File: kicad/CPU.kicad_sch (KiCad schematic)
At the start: 37 parts, among them J1 Conn_ARM_SWD_TagConnect_TC203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, J2 Screw_Terminal_01x03, J3 Screw_Terminal_01x03, SW1 SW_Push, U7 STM32F303CBTx, U8 ATA6560-GAQW-N, Y1 8 MHz

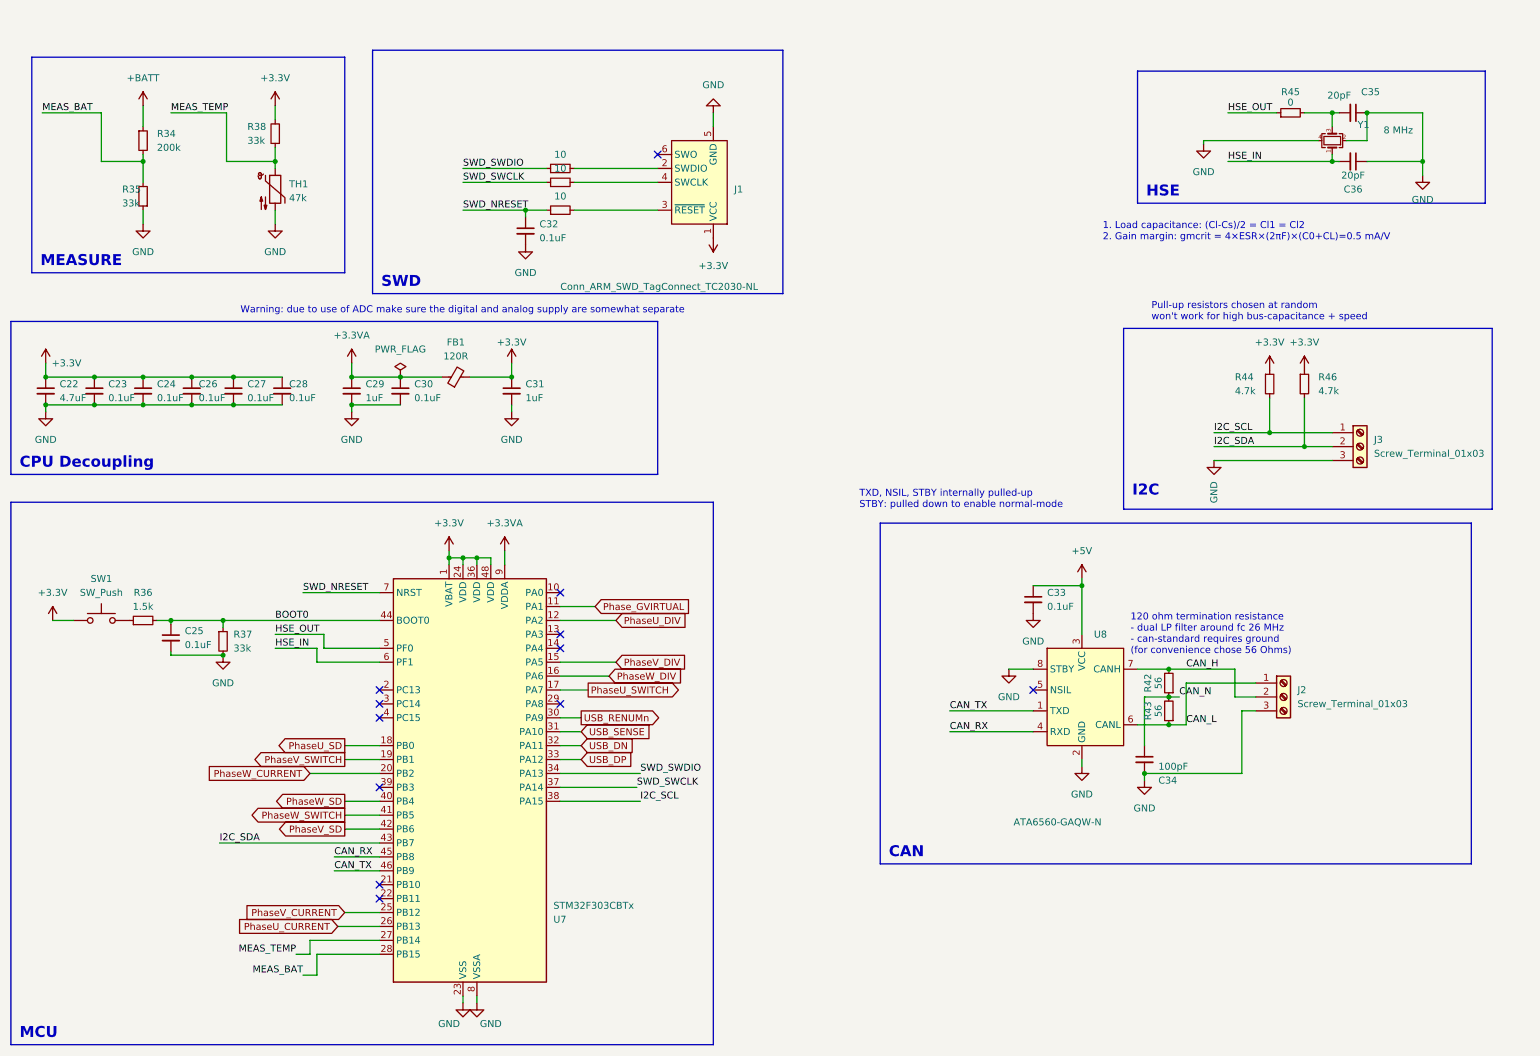
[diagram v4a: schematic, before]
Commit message: [kicad] Added testpoints, added 1 amp fuses at 2 buck converters
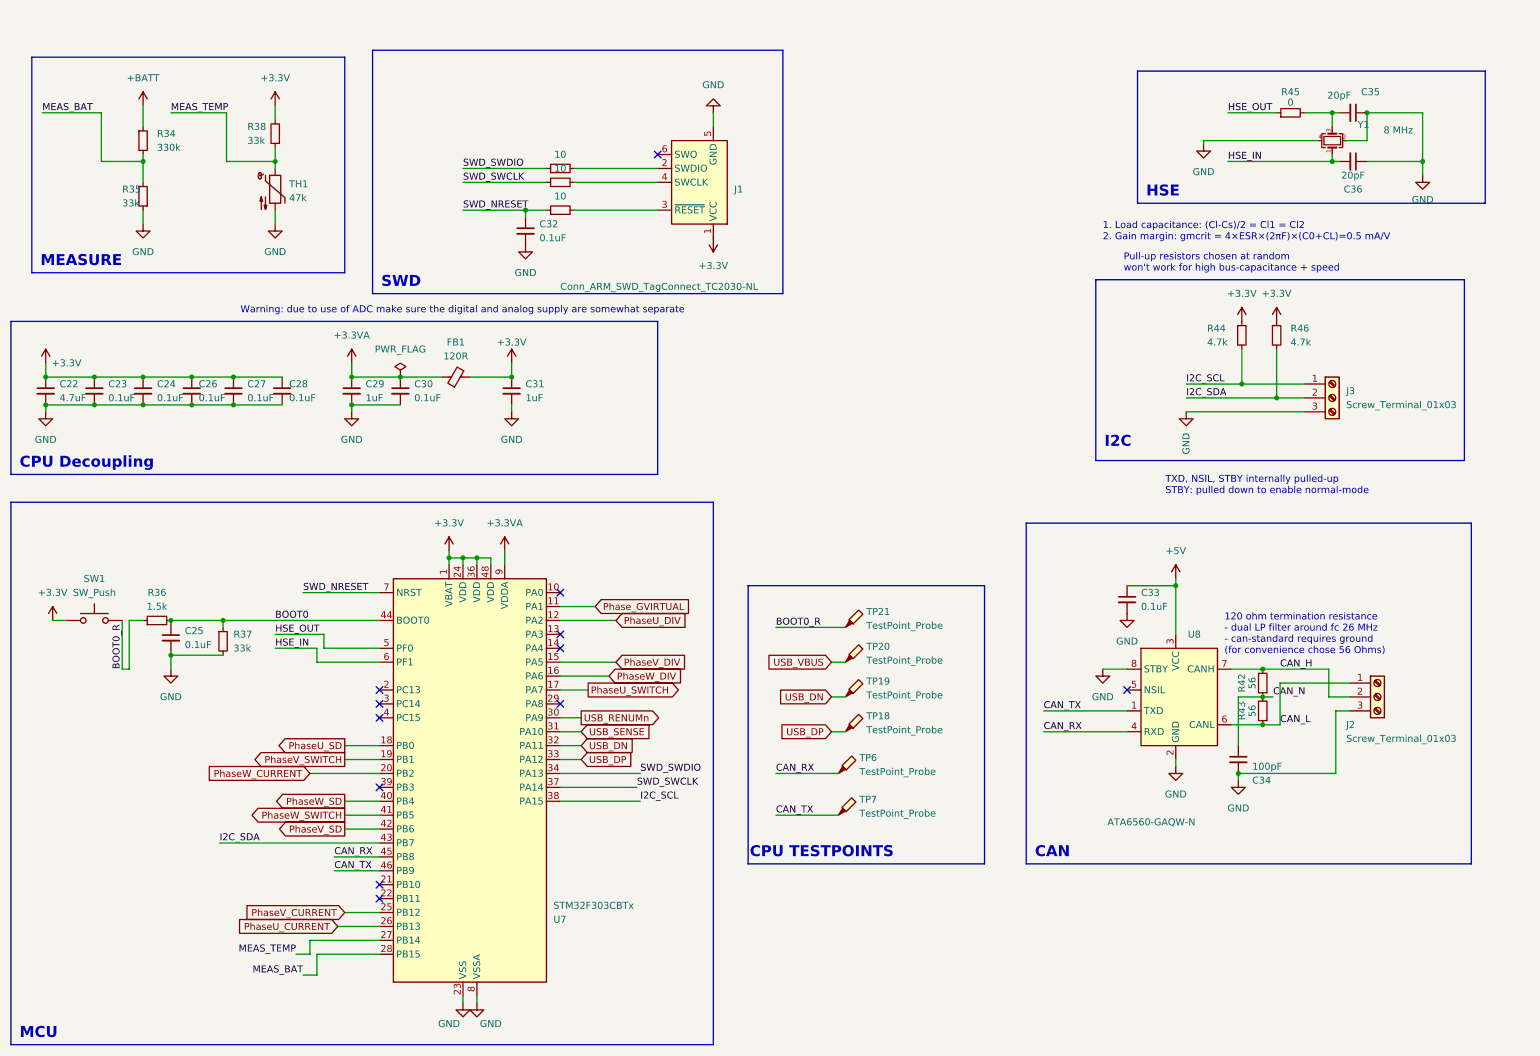
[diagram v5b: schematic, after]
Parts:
- added TP18, TP19, TP20, TP21, TP6, TP7: TestPoint_Probe, TestPoint:TestPoint_THTPad_D1.0mm_Drill0.5mm, symbol Connector:TestPoint_Probe
- R34: value 200k -> 330k; MFR.Part 0603WAF2003T5E -> 0603WAF3303T5E; jlcpcb C25811 -> C23137
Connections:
- net CAN_RX: now also TP6.1
- net CAN_TX: now also TP7.1
- net USB_DN: now also TP19.1
- net USB_DP: now also TP18.1
- net BOOT0_R: now reaches R36.1, SW1.2
- net BOOT0_R: now also TP21.1
- new net USB_VBUS: TP20.1
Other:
- moved on the sheet: C33, C34, J2, J3, R36, R42, R43, R44, R46, SW1, U8

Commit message: [kicad] Added power and keepalive LED | TODO: Add extra mcu output
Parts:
- added D8: LED, LED_SMD:LED_0805_2012Metric, symbol Device:LED
- added R51: 1.5k, Resistor_SMD:R_0805_2012Metric, symbol Device:R_Small
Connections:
- net GND: now also D8.1 (K)
- net at U7.2 (PC13): now also R51.2
- new net: D8.2 (A), R51.1
- no-connect marks 12 -> 11
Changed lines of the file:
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@@
   (no_connect (at 114.3 123.19))
   (no_connect (at 132.08 33.02))
-  (no_connect (at 81.28 130.81))
   (no_connect (at 81.28 168.91))
   (no_connect (at 81.28 135.89))
@@
     (stroke (width 0) (type default))
   )
+  (wire (pts (xy 64.135 130.81) (xy 66.675 130.81))
+    (stroke (width 0) (type default))
+  )
   (wire (pts (xy 38.1 34.29) (xy 30.48 34.29))
     (stroke (width 0) (type default))
@@
     (stroke (width 0) (type default))
   )
+  (wire (pts (xy 52.705 130.81) (xy 56.515 130.81))
+    (stroke (width 0) (type default))
+  )
   (wire (pts (xy 93.98 105.41) (xy 93.98 106.68))
     (stroke (width 0) (type default))
@@
     (stroke (width 0) (type default))
   )
+  (wire (pts (xy 52.705 132.715) (xy 52.705 130.81))
+    (stroke (width 0) (type default))
+  )
   (wire (pts (xy 261.62 34.29) (xy 271.78 34.29))
     (stroke (width 0) (type default))
@@
   )
   (wire (pts (xy 71.12 123.19) (xy 81.28 123.19))
+    (stroke (width 0) (type default))
+  )
+  (wire (pts (xy 71.755 130.81) (xy 81.28 130.81))
     (stroke (width 0) (type default))
   )
@@
         (path "/91e2f46a-700b-4d7a-a06a-22469f63223f/7eb1e86b-8a48-408f-b231-0c52f4ea1971"
           (reference "TH1") (unit 1)
+        )
+      )
+    )
+  )
+  (symbol (lib_id "Device:LED") (at 60.325 130.81 0) (unit 1)
+    (in_bom yes) (on_board yes) (dnp no)
+    (property "Reference" "D8" (at 59.69 125.73 0)
+      (effects (font (size 1.27 1.27)))
+    )
+    (property "Value" "LED" (at 60.325 128.27 0)
+      (effects (font (size 1.27 1.27)))
+    )
+    (property "Footprint" "LED_SMD:LED_0805_2012Metric" (at 60.325 130.81 0)
+      (effects (font (size 1.27 1.27)) hide)
+    )
+    (property "Datasheet" "https://wmsc.lcsc.com/wmsc/upload/file/pdf/v2/lcsc/2106081832_baizou-BZ-C0805-Y2-E1_C2833070.pdf" (at 60.325 130.81 0)
+      (effects (font (size 1.27 1.27)) hide)
+    )
+    (property "jlcpcb" "C2833070" (at 60.325 130.81 0)
+      (effects (font (size 1.27 1.27)) hide)
+    )
+    (property "MFR.Part" "BZ-C0805-Y2-E1" (at 60.325 130.81 0)
+      (effects (font (size 1.27 1.27)) hide)
+    )
+    (pin "1")
+    (pin "2")
+    (instances
+      (project "bldc_project"
+        (path "/91e2f46a-700b-4d7a-a06a-22469f63223f/7eb1e86b-8a48-408f-b231-0c52f4ea1971"
+          (reference "D8") (unit 1)
         )
       )
@@
         )
       )
+    )
+  )
+  (symbol (lib_id "Device:R_Small") (at 69.215 130.81 90) (unit 1)
+    (in_bom yes) (on_board yes) (dnp no)
+    (property "Reference" "R51" (at 67.31 126.365 90)
+      (effects (font (size 1.27 1.27)))
+    )
+    (property "Value" "1.5k" (at 67.945 128.27 90)
+      (effects (font (size 1.27 1.27)))
+    )
+    (property "Footprint" "Resistor_SMD:R_0805_2012Metric" (at 69.215 130.81 0)
+      (effects (font (size 1.27 1.27)) hide)
+    )
+    (property "Datasheet" "https://wmsc.lcsc.com/wmsc/upload/file/pdf/v2/lcsc/2206010216_UNI-ROYAL-Uniroyal-Elec-0805W8F1501T5E_C4310.pdf" (at 69.215 130.81 0)
+      (effects (font (size 1.27 1.27)) hide)
+    )
+    (property "jlcpcb" "C4310" (at 69.215 130.81 0)
+      (effects (font (size 1.27 1.27)) hide)
+    )
+    (property "MFR.Part" "0805W8F1501T5E" (at 69.215 130.81 0)
+      (effects (font (size 1.27 1.27)) hide)
+    )
+    (pin "2")
+    (pin "1")
+    (instances
+      (project "bldc_project"
+        (path "/91e2f46a-700b-4d7a-a06a-22469f63223f/7eb1e86b-8a48-408f-b231-0c52f4ea1971"
+          (reference "R51") (unit 1)
+        )
+      )
+    )
+  )
+  (symbol (lib_id "OLIMEX_Power:GND") (at 52.705 132.715 0) (unit 1)
+    (in_bom yes) (on_board yes) (dnp no) (fields_autoplaced)
+    (property "Reference" "#PWR068" (at 52.705 139.065 0)
+      (effects (font (size 1.27 1.27)) hide)
+    )
+    (property "Value" "GND" (at 52.705 137.795 0)
+      (effects (font (size 1.27 1.27)))
+    )
+    (property "Footprint" "" (at 52.705 132.715 0)
+      (effects (font (size 1.524 1.524)))
+    )
+    (property "Datasheet" "" (at 52.705 132.715 0)
+      (effects (font (size 1.524 1.524)))
+    )
+    (pin "1")
+    (instances
+      (project "bldc_project"
+        (path "/91e2f46a-700b-4d7a-a06a-22469f63223f/7eb1e86b-8a48-408f-b231-0c52f4ea1971"
+          (reference "#PWR068") (unit 1)
+        )
+      )
